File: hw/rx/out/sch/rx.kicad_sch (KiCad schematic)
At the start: 0 parts

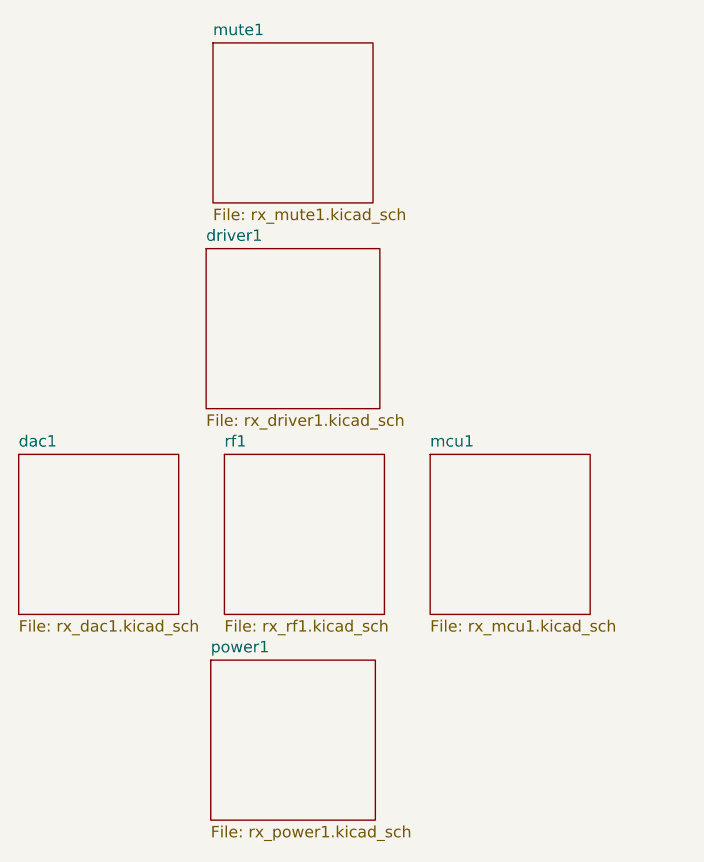
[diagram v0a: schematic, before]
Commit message: hw/rx: receiver sub-board layout, 50 ohm GCPW, keyed J1, JLC rules that load, fab outputs (#34) (#116)
Part of #34. Receiver layout (48x90 mm, DRC 0/0), #116 independent-review fixes (netclass pour clearances in rx + pack, no hole at J1 pin 14, solid RF grounds, K1 pin-1/CPL), every placed part with a checked LCSC code.

Co-Authored-By: Claude Opus 5.5 <noreply@anthropic.com>
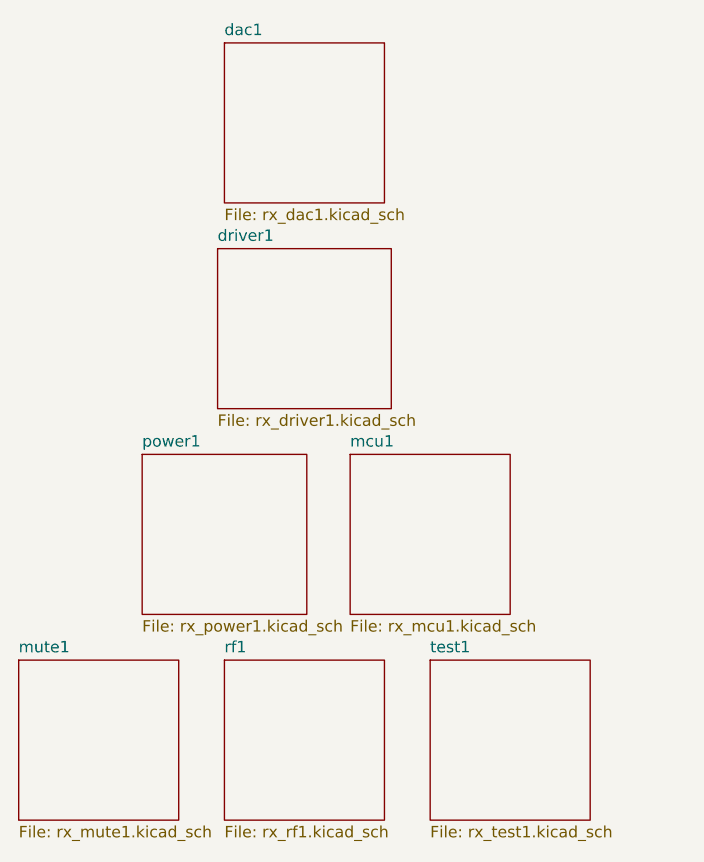
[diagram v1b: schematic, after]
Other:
- added sheet test1 (rx_test1.kicad_sch)
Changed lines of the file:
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@@
     (comment 4 ""))
   (sheet
-    (at 138.18 130.81)
+    (at 130.56 107.95)
     (size 18.29 17.78)
     (exclude_from_sim no)
@@
       (color 0 0 0 0.0))
     (property "Sheetname" "power1"
-      (at 138.18 130.1 0)
+      (at 130.56 107.24 0)
       (effects
         (font
@@
         (justify left bottom)))
     (property "Sheetfile" "rx_power1.kicad_sch"
-      (at 138.18 149.17 0)
+      (at 130.56 126.31 0)
       (effects
         (font
@@
         (justify left top))))
   (sheet
-    (at 162.56 107.95)
+    (at 153.67 107.95)
     (size 17.78 17.78)
     (exclude_from_sim no)
@@
       (color 0 0 0 0.0))
     (property "Sheetname" "mcu1"
-      (at 162.56 107.24 0)
+      (at 153.67 107.24 0)
       (effects
         (font
@@
         (justify left bottom)))
     (property "Sheetfile" "rx_mcu1.kicad_sch"
-      (at 162.56 126.31 0)
+      (at 153.67 126.31 0)
       (effects
         (font
@@
         (justify left top))))
   (sheet
-    (at 139.7 107.95)
+    (at 139.7 130.81)
     (size 17.78 17.78)
     (exclude_from_sim no)
@@
       (color 0 0 0 0.0))
     (property "Sheetname" "rf1"
-      (at 139.7 107.24 0)
+      (at 139.7 130.1 0)
       (effects
         (font
@@
         (justify left bottom)))
     (property "Sheetfile" "rx_rf1.kicad_sch"
-      (at 139.7 126.31 0)
+      (at 139.7 149.17 0)
       (effects
         (font
@@
         (justify left top))))
   (sheet
-    (at 116.84 107.95)
+    (at 139.7 62.23)
     (size 17.78 17.78)
     (exclude_from_sim no)
@@
       (color 0 0 0 0.0))
     (property "Sheetname" "dac1"
-      (at 116.84 107.24 0)
+      (at 139.7 61.52 0)
       (effects
         (font
@@
         (justify left bottom)))
     (property "Sheetfile" "rx_dac1.kicad_sch"
-      (at 116.84 126.31 0)
+      (at 139.7 80.59 0)
       (effects
         (font
@@
         (justify left top))))
   (sheet
-    (at 137.67 85.09)
+    (at 138.94 85.09)
     (size 19.3 17.78)
     (exclude_from_sim no)
@@
       (color 0 0 0 0.0))
     (property "Sheetname" "driver1"
-      (at 137.67 84.38 0)
+      (at 138.94 84.38 0)
       (effects
         (font
@@
         (justify left bottom)))
     (property "Sheetfile" "rx_driver1.kicad_sch"
-      (at 137.67 103.45 0)
+      (at 138.94 103.45 0)
       (effects
         (font
@@
         (justify left top))))
   (sheet
-    (at 138.43 62.23)
+    (at 116.84 130.81)
     (size 17.78 17.78)
     (exclude_from_sim no)
@@
       (color 0 0 0 0.0))
     (property "Sheetname" "mute1"
-      (at 138.43 61.52 0)
+      (at 116.84 130.1 0)
       (effects
         (font
@@
         (justify left bottom)))
     (property "Sheetfile" "rx_mute1.kicad_sch"
-      (at 138.43 80.59 0)
+      (at 116.84 149.17 0)
       (effects
         (font
+          (size 1.27 1.27))
+        (justify left top))))
+  (sheet
+    (at 162.56 130.81)
+    (size 17.78 17.78)
+    (exclude_from_sim no)
+    (in_bom yes)
+    (on_board yes)
+    (dnp no)
+    (fields_autoplaced yes)
+    (stroke
+      (width 0.1524)
+      (type solid))
+    (fill
+      (color 0 0 0 0.0))
+    (property "Sheetname" "test1"
+      (at 162.56 130.1 0)
+      (effects
+        (font
+          (size 1.27 1.27))
+        (justify left bottom)))
+    (property "Sheetfile" "rx_test1.kicad_sch"
+      (at 162.56 149.17 0)
+      (effects
+        (font
